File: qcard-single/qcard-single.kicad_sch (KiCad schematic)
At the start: 4 parts, among them J1 QCard_Conn, U1 SST39SF040

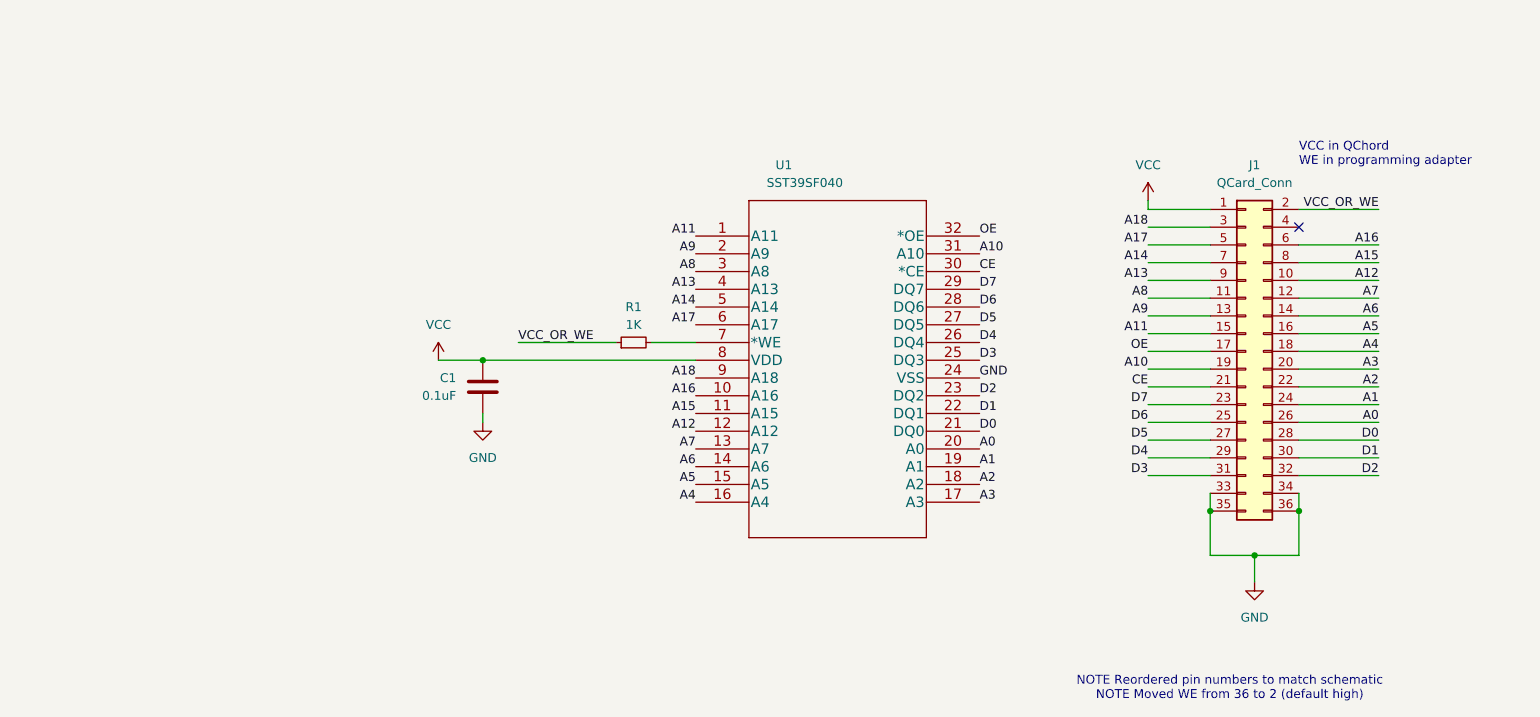
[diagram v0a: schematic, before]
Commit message: Replace qcard-tsop32
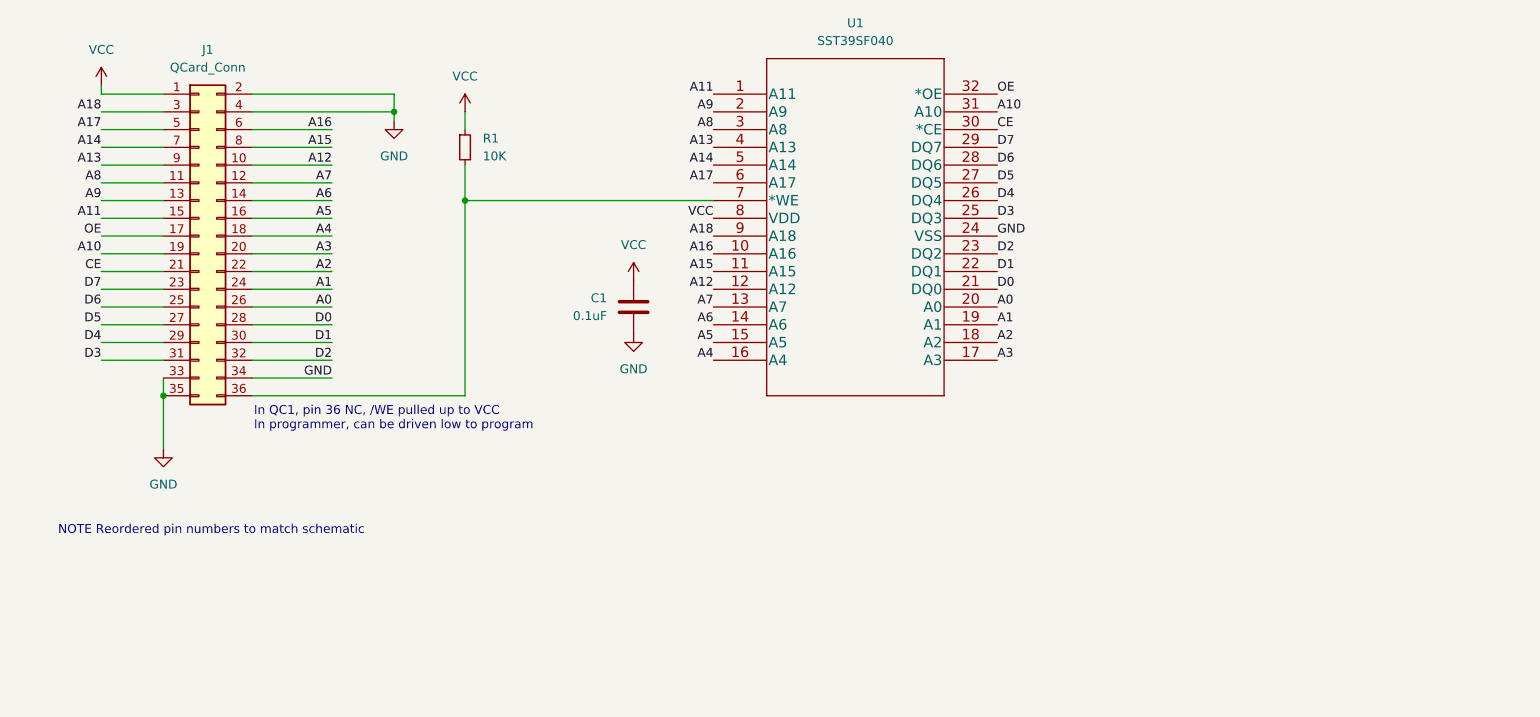
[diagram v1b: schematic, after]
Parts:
- R1: value 1K -> 10K
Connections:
- net GND: now also J1.2 (Pin_2), J1.4 (Pin_4); no longer J1.36 (Pin_36)
- net VCC: now also R1.1
- net at R1.2, U1.7 (*WE): now also J1.36 (Pin_36)
- removed net VCC_OR_WE: J1.2 (Pin_2), R1.1
- no-connect marks 1 -> 0
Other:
- note added: "In QC1, pin 36 NC, /WE pulled up to VCC In programmer, can be driven low to program"
- note added: "NOTE Reordered pin numbers to match schematic"
- note removed: "NOTE Reordered pin numbers to match schematic NOTE Moved WE from 36 to 2 (default high)"
- note removed: "VCC in QChord WE in programming adapter"
- moved on the sheet: J1, U1
